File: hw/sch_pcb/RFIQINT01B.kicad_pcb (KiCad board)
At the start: 2 copper layers, 60.5 x 50.3 mm, 48 parts, among them J1 Umin ... Umax, J2 SATA7-67491-1030, J3 HEADER_1x08, J4 SATA7-67491-1030, J5 HEADER_1x08, J6 SATA7-67491-1030, M1 HOLE, M2 HOLE, M3 HOLE, M4 HOLE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

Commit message: Edit. #3  #2
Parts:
- C1: footprint Capacitors_SMD:C_1210_HandSoldering -> Capacitor_SMD:C_0805_2012Metric
- C10, C11, C12, C13, C14, C15, C16, C2, C3, C4, C5, C6, C7, C8, C9: footprint Mlab_C:SMD-0603 -> Capacitor_SMD:C_0603_1608Metric
- C17: value 10uF -> 10uF/16V; footprint Mlab_C:C_0805 -> Capacitor_SMD:C_0805_2012Metric
- D1: footprint Diodes_SMD:D_SMA -> Diode_SMD:D_SMA
- J1: value Umin ... Umax -> HEADER_2x04_PARALLEL; footprint Mlab_Pin_Headers:Straight_2x03 -> Mlab_Pin_Headers:Straight_2x04
- J2, J4, J6: footprint Connectors:SATA-7_THT_VERT_2 -> Mlab_CON:SATA-7_THT_VERT_2
- J3, J5: footprint maxrez:IDC381-8-110 -> Mlab_CON:IDC381-8-110
- R1, R10, R11, R12, R13, R14, R2, R3, R4, R5, R6, R7, R8, R9: footprint Mlab_R:SMD-0603 -> Resistor_SMD:R_0603_1608Metric
- U1, U2: footprint Housings_SOIC:SOIC-8_3.9x4.9mm_Pitch1.27mm -> Package_SO:SOIC-8_3.9x4.9mm_P1.27mm
- U3: footprint TO_SOT_Packages_SMD:SOT-223-3_TabPin2 -> Package_TO_SOT_SMD:SOT-223-3_TabPin2
- moved C1 5.18 mm to (147.9, 111.8), turned to 180 degrees
- moved C2 4.90 mm to (147.9, 114.7), turned to 180 degrees
- moved D1 3.77 mm to (151.5, 108.0)
- moved J1 2.98 mm to (152.8, 116.1), turned to 0 degrees
- turned J5 to 90 degrees
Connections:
- J1 pad 5: GND -> VCC
- J1 pad 6: GND -> VCC
- J5 pad 1: /CLK_OUT2_N -> VCC
- J5 pad 2: /CLK_OUT2_P -> GND
- J5 pad 3: /ADC4_N -> /ADC3_P
- J5 pad 4: /ADC4_P -> /ADC3_N
- J5 pad 5: /ADC3_N -> /ADC4_P
- J5 pad 6: /ADC3_P -> /ADC4_N
- J5 pad 7: GND -> /CLK_OUT2_P
- J5 pad 8: VCC -> /CLK_OUT2_N
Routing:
- net VCC: track 89.2 -> 93.6 mm
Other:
- board text removed: "J1"

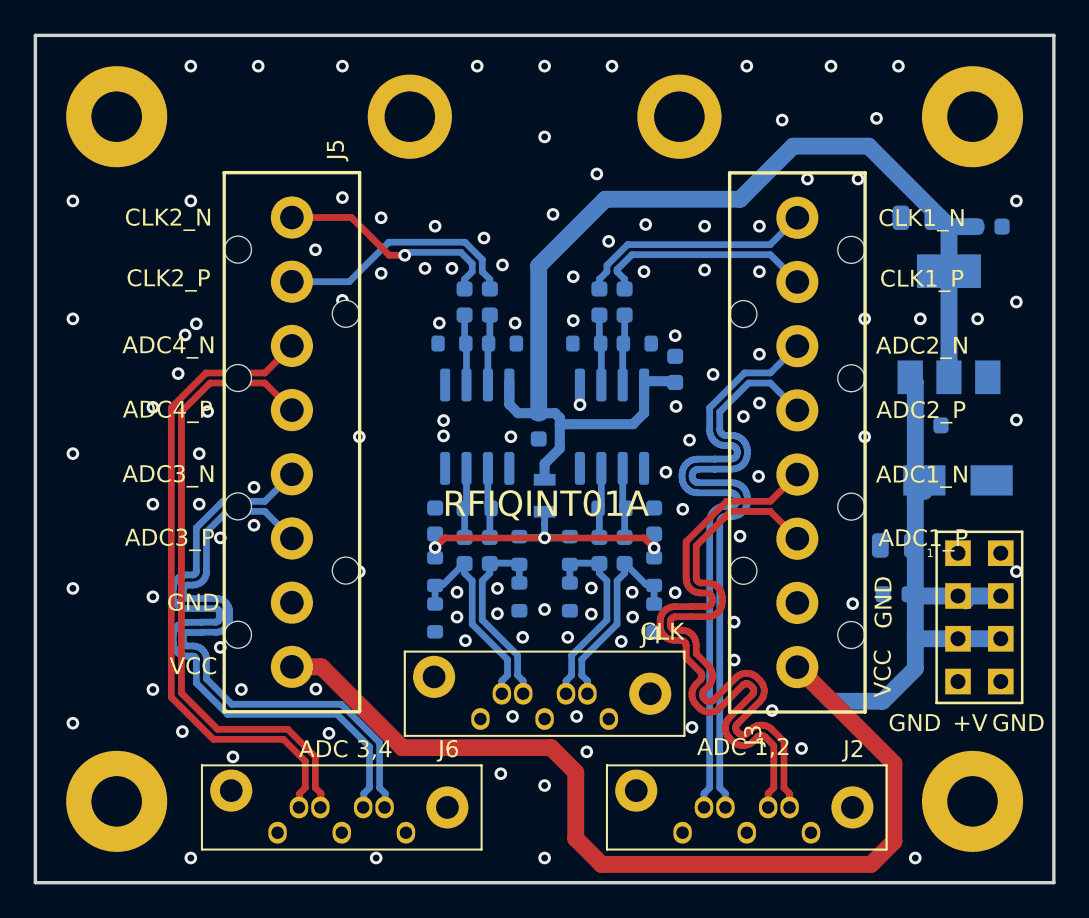
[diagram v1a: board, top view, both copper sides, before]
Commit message: Fix differential pair routing #3.
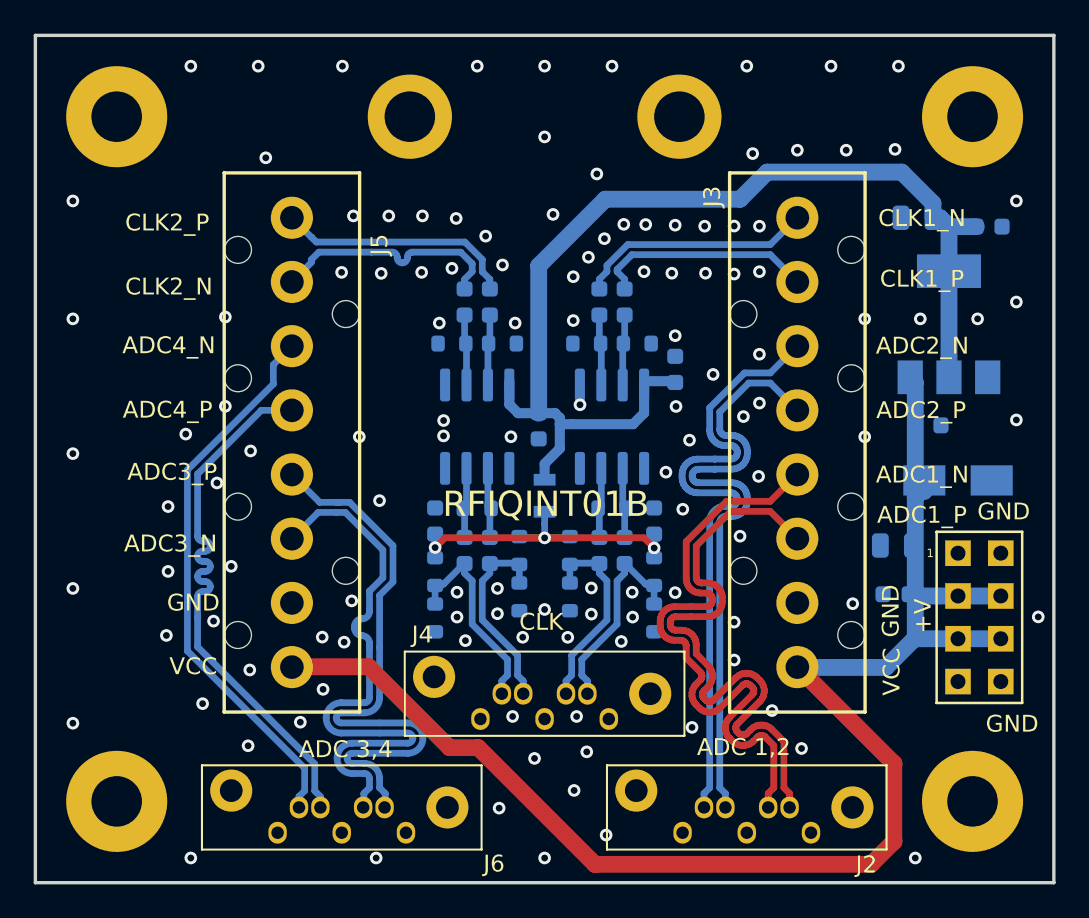
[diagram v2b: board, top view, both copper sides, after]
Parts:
- R1, R13, R14, R2: value 83 -> 82
- R10, R12, R3, R5, R6, R7, R8, R9: value 127 -> 130
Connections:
- J5 pad 3: /ADC3_P -> /ADC3_N
- J5 pad 4: /ADC3_N -> /ADC3_P
- J5 pad 7: /CLK_OUT2_P -> /CLK_OUT2_N
- J5 pad 8: /CLK_OUT2_N -> /CLK_OUT2_P
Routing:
- net VCC: track 93.6 -> 88.1 mm
- net /ADC4_N: track 38.1 -> 33.0 mm
- net /ADC4_P: track 37.1 -> 32.8 mm
- net /ADC3_N: track 38.1 -> 35.3 mm
- net +3V3: track 67.5 -> 65.6 mm
- net /ADC3_P: track 37.1 -> 35.7 mm
- net /CLK_OUT2_N: track 13.7 -> 14.2 mm, vias 1 -> 0
- net GND: vias 117 -> 123
- net (no net): vias 1 -> 0
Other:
- board text added: "RFIQINT01B"
- board text removed: "RFIQINT01A"

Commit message: Edit PCB
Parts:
- moved R2 0.40 mm to (128.3, 115.2)
- moved R13 0.40 mm to (125.7, 115.2)
- moved R1 0.32 mm to (133.5, 116.4)
- moved R14 0.27 mm to (120.5, 116.4)
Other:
- board text added: "MLAB.CZ 2022"
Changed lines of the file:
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@@
     )
     (pad_to_mask_clearance 0.2)
-    (solder_mask_min_width 0.25)
     (pcbplotparams
       (layerselection 0x0000030_80000001)
@@
     (property "UST_ID" "5c70984712875079b91f8b81")
     (attr smd)
-    (fp_text reference "U1" (at 0 3.4 270) (layer "B.SilkS")
+    (fp_text reference "U1" (at -0.2944 3.5184 270) (layer "B.SilkS")
       (effects (font (size 1 1) (thickness 0.15)) (justify mirror))
     )
@@
     (property "UST_ID" "5c70984712875079b91f8b81")
     (attr smd)
-    (fp_text reference "U2" (at 0 3.4 270) (layer "B.SilkS")
+    (fp_text reference "U2" (at -0.0404 -3.62 270) (layer "B.SilkS")
       (effects (font (size 1 1) (thickness 0.15)) (justify mirror))
     )
@@
     (property "UST_ID" "5c70984812875079b91f8bbe")
     (attr smd)
-    (fp_text reference "C1" (at 0 1.68) (layer "B.SilkS")
+    (fp_text reference "C1" (at 0.6604 1.68) (layer "B.SilkS")
       (effects (font (size 1 1) (thickness 0.15)) (justify mirror))
     )
@@
   )
   (footprint "Resistor_SMD:R_0603_1608Metric" (layer "B.Cu")
-    (at 133.5 116.11 90)
+    (at 133.5024 116.4336 90)
     (descr "Resistor SMD 0603 (1608 Metric), square (rectangular) end terminal, IPC_7351 nominal, (Body size source: IPC-SM-782 page 72, https://www.pcb-3d.com/wordpress/wp-content/uploads/ipc-sm-782a_amendment_1_and_2.pdf), generated with kicad-footprint-generator")
     (tags "resistor")
@@
   )
   (footprint "Resistor_SMD:R_0603_1608Metric" (layer "B.Cu")
-    (at 128.5 114.86 90)
+    (at 128.3208 115.2144 90)
     (descr "Resistor SMD 0603 (1608 Metric), square (rectangular) end terminal, IPC_7351 nominal, (Body size source: IPC-SM-782 page 72, https://www.pcb-3d.com/wordpress/wp-content/uploads/ipc-sm-782a_amendment_1_and_2.pdf), generated with kicad-footprint-generator")
     (tags "resistor")
@@
     (property "UST_ID" "5cd08b17128750448e4542b1")
     (attr smd)
-    (fp_text reference "R3" (at 0 1.43) (layer "B.SilkS")
+    (fp_text reference "R3" (at -1.104 1.3766) (layer "B.SilkS")
       (effects (font (size 1 1) (thickness 0.15)) (justify mirror))
     )
@@
     (property "UST_ID" "5c70984512875079b91f8956")
     (attr smd)
-    (fp_text reference "R4" (at 0 1.43) (layer "B.SilkS")
+    (fp_text reference "R4" (at 0 1.43) (layer "B.SilkS") hide
       (effects (font (size 1 1) (thickness 0.15)) (justify mirror))
     )
@@
     (property "UST_ID" "5cd08b17128750448e4542b1")
     (attr smd)
-    (fp_text reference "R6" (at 2.51 0.25 270) (layer "B.SilkS")
+    (fp_text reference "R6" (at 2.51 0.25 270) (layer "B.SilkS") hide
       (effects (font (size 1 1) (thickness 0.15)) (justify mirror))
     )
@@
     (property "UST_ID" "5cd08b17128750448e4542b1")
     (attr smd)
-    (fp_text reference "R7" (at 0 1.43) (layer "B.SilkS")
+    (fp_text reference "R7" (at 0 1.43) (layer "B.SilkS") hide
       (effects (font (size 1 1) (thickness 0.15)) (justify mirror))
     )
@@
     (property "UST_ID" "5cd08b17128750448e4542b1")
     (attr smd)
-    (fp_text reference "R8" (at 0 1.43 90) (layer "B.SilkS")
+    (fp_text reference "R8" (at 0 1.43 90) (layer "B.SilkS") hide
       (effects (font (size 1 1) (thickness 0.15)) (justify mirror))
     )
@@
     (property "UST_ID" "5cd08b17128750448e4542b1")
     (attr smd)
-    (fp_text reference "R10" (at 0 1.43) (layer "B.SilkS")
+    (fp_text reference "R10" (at -1.8396 1.529) (layer "B.SilkS")
       (effects (font (size 1 1) (thickness 0.15)) (justify mirror))
     )
@@
     (property "UST_ID" "5c70984512875079b91f8956")
     (attr smd)
-    (fp_text reference "R11" (at 0 1.43) (layer "B.SilkS")
+    (fp_text reference "R11" (at 0 1.43) (layer "B.SilkS") hide
       (effects (font (size 1 1) (thickness 0.15)) (justify mirror))
     )
@@
     (property "UST_ID" "5cd08b17128750448e4542b1")
     (attr smd)
-    (fp_text reference "R12" (at 0 1.43) (layer "B.SilkS")
+    (fp_text reference "R12" (at 3.136 0.005) (layer "B.SilkS")
       (effects (font (size 1 1) (thickness 0.15)) (justify mirror))
     )
@@
   )
   (footprint "Resistor_SMD:R_0603_1608Metric" (layer "B.Cu")
-    (at 125.5 114.86 -90)
+    (at 125.6792 115.2144 -90)
     (descr "Resistor SMD 0603 (1608 Metric), square (rectangular) end terminal, IPC_7351 nominal, (Body size source: IPC-SM-782 page 72, https://www.pcb-3d.com/wordpress/wp-content/uploads/ipc-sm-782a_amendment_1_and_2.pdf), generated with kicad-footprint-generator")
     (tags "resistor")
@@
     (property "UST_ID" "5c70984512875079b91f8955")
     (attr smd)
-    (fp_text reference "R13" (at 0 1.43 90) (layer "B.SilkS")
+    (fp_text reference "R13" (at 0.2528 1.4464 90) (layer "B.SilkS")
       (effects (font (size 1 1) (thickness 0.15)) (justify mirror))
     )
@@
   )
   (footprint "Resistor_SMD:R_0603_1608Metric" (layer "B.Cu")
-    (at 120.5 116.11 -90)
+    (at 120.4976 116.3828 -90)
     (descr "Resistor SMD 0603 (1608 Metric), square (rectangular) end terminal, IPC_7351 nominal, (Body size source: IPC-SM-782 page 72, https://www.pcb-3d.com/wordpress/wp-content/uploads/ipc-sm-782a_amendment_1_and_2.pdf), generated with kicad-footprint-generator")
     (tags "resistor")
@@
     (property "UST_ID" "5c70984812875079b91f8bf2")
     (attr smd)
-    (fp_text reference "C5" (at 0 1.43 90) (layer "B.SilkS")
+    (fp_text reference "C5" (at -0.4844 -1.7016 90) (layer "B.SilkS")
       (effects (font (size 1 1) (thickness 0.15)) (justify mirror))
     )
@@
     (property "UST_ID" "5c70984812875079b91f8bf2")
     (attr smd)
-    (fp_text reference "C10" (at 0 1.43 90) (layer "B.SilkS")
+    (fp_text reference "C10" (at 0.2936 1.6312 90) (layer "B.SilkS") hide
       (effects (font (size 1 1) (thickness 0.15)) (justify mirror))
     )
@@
     (property "UST_ID" "5c70984812875079b91f8bf2")
     (attr smd)
-    (fp_text reference "C11" (at 0 1.43 90) (layer "B.SilkS")
+    (fp_text reference "C11" (at 0 1.43 90) (layer "B.SilkS") hide
       (effects (font (size 1 1) (thickness 0.15)) (justify mirror))
     )
@@
     (property "UST_ID" "5c70984812875079b91f8bf2")
     (attr smd)
-    (fp_text reference "C12" (at 0 1.43 90) (layer "B.SilkS")
+    (fp_text reference "C12" (at -1.348 -1.9292 90) (layer "B.SilkS")
       (effects (font (size 1 1) (thickness 0.15)) (justify mirror))
     )
@@
     (property "UST_ID" "5c70984812875079b91f8bf2")
     (attr smd)
-    (fp_text reference "C13" (at 0 1.43 90) (layer "B.SilkS")
+    (fp_text reference "C13" (at 0 1.43 90) (layer "B.SilkS") hide
       (effects (font (size 1 1) (thickness 0.15)) (justify mirror))
     )
@@
     (property "UST_ID" "5c70984812875079b91f8bf2")
     (attr smd)
-    (fp_text reference "C14" (at 0 1.43 90) (layer "B.SilkS")
+    (fp_text reference "C14" (at -0.586 1.5492 90) (layer "B.SilkS")
       (effects (font (size 1 1) (thickness 0.15)) (justify mirror))
     )
@@
     (property "UST_ID" "5c70984812875079b91f8bf2")
     (attr smd)
-    (fp_text reference "C15" (at 0 1.43) (layer "B.SilkS")
+    (fp_text reference "C15" (at -3.158 -0.0188) (layer "B.SilkS")
       (effects (font (size 1 1) (thickness 0.15)) (justify mirror))
     )
@@
     (property "UST_ID" "5c70984812875079b91f8bf2")
     (attr smd)
-    (fp_text reference "C16" (at 0 1.43) (layer "B.SilkS")
+    (fp_text reference "C16" (at 0.1622 1.6482) (layer "B.SilkS")
       (effects (font (size 1 1) (thickness 0.15)) (justify mirror))
     )
@@
     (property "UST_ID" "5c70984812875079b91f8bbe")
     (attr smd)
-    (fp_text reference "C17" (at 0 1.68 180) (layer "B.SilkS")
+    (fp_text reference "C17" (at -3.6596 -0.0564 180) (layer "B.SilkS")
       (effects (font (size 1 1) (thickness 0.15)) (justify mirror))
     )
@@
     (effects (font (size 1 1) (thickness 0.15)))
   )
+  (gr_text "MLAB.CZ\n2022" (at 127.075 98.6028) (layer "F.SilkS")
+    (effects (font (size 1.5 1.5) (thickness 0.3)))
+  )
   (gr_text "VCC" (at 106.15 118.985) (layer "F.SilkS")
